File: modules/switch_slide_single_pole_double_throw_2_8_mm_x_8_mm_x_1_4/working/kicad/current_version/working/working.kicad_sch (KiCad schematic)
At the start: 1 part, among them J1 sws2880

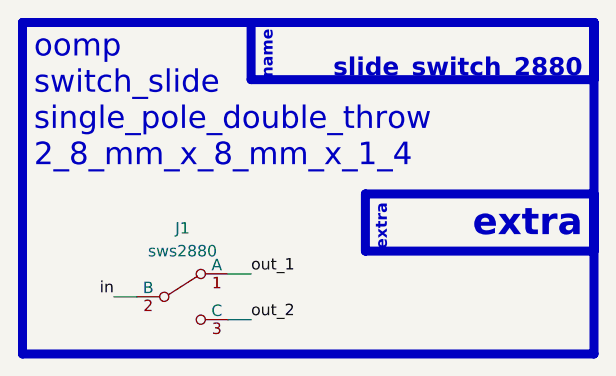
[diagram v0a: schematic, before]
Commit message: fixed formatting to be more consistent
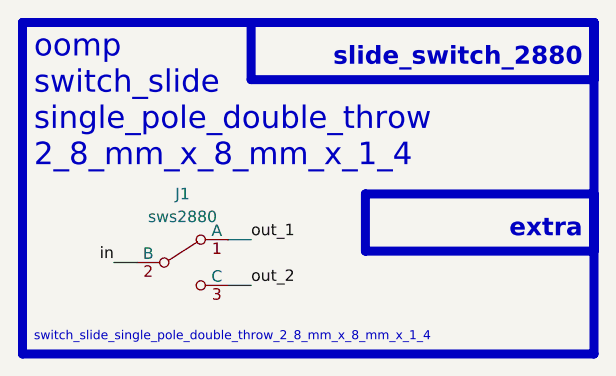
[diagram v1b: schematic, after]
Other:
- note added: "switch_slide_single_pole_double_throw_2_8_mm_x_8_mm_x_1_4"
- note removed: "name"
- moved on the sheet: J1
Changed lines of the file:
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@@
 (kicad_sch (version 20230121) (generator eeschema)
   (paper "A4")
-  (wire (pts (xy 116.84 86.36) (xy 119.38 86.36))
+  (wire (pts (xy 116.84 82.55) (xy 119.38 82.55))
     (stroke (width 0) (type default))
   )
-  (wire (pts (xy 129.54 88.9) (xy 132.08 88.9))
+  (wire (pts (xy 129.54 85.09) (xy 132.08 85.09))
     (stroke (width 0) (type default))
   )
-  (wire (pts (xy 129.54 83.82) (xy 132.08 83.82))
+  (wire (pts (xy 129.54 80.01) (xy 132.08 80.01))
     (stroke (width 0) (type default))
   )
   (rectangle (start 132.08 55.88) (end 170.18 62.23)
     (stroke (width 1) (type default))
-    (fill (type color) (color 0 0 0 0))
+    (fill (type none))
   )
   (rectangle (start 106.68 55.88) (end 170.18 92.71)
@@
     (fill (type none))
   )
-  (text "name" (at 134.62 62.23 90)
-    (effects (font (size 1.27 1.27) (thickness 0.254) bold (color 255 255 255 1)) (justify left bottom))
+  (text "slide_switch_2880" (at 168.91 60.96 0)
+    (effects (font (size 2 2) (thickness 0.8) bold) (justify right bottom))
   )
-  (text "slide_switch_2880" (at 168.91 62.23 0)
-    (effects (font (size 2 2) (thickness 0.8) bold (color 255 255 255 1)) (justify right bottom))
-  )
-  (text "extra" (at 147.32 81.28 90)
-    (effects (font (size 1.27 1.27) (thickness 0.254) bold) (justify left bottom))
+  (text "switch_slide_single_pole_double_throw_2_8_mm_x_8_mm_x_1_4"
+    (at 107.95 91.44 0)
+    (effects (font (size 1 1)) (justify left bottom))
   )
   (text "extra" (at 168.91 80.01 0)
-    (effects (font (size 3 3) (thickness 0.8) bold) (justify right bottom))
+    (effects (font (size 2 2) (thickness 0.8) bold) (justify right bottom))
   )
   (text "oomp\nswitch_slide\nsingle_pole_double_throw\n2_8_mm_x_8_mm_x_1_4\n\n"
@@
     (effects (font (size 2.5 2.5)) (justify left bottom))
   )
-  (label "out_1" (at 132.08 83.82 0) (fields_autoplaced)
+  (label "out_1" (at 132.08 80.01 0) (fields_autoplaced)
     (effects (font (size 1.27 1.27)) (justify left bottom))
   )
-  (label "out_2" (at 132.08 88.9 0) (fields_autoplaced)
+  (label "out_2" (at 132.08 85.09 0) (fields_autoplaced)
     (effects (font (size 1.27 1.27)) (justify left bottom))
   )
-  (label "in" (at 116.84 86.36 180) (fields_autoplaced)
+  (label "in" (at 116.84 82.55 180) (fields_autoplaced)
     (effects (font (size 1.27 1.27)) (justify right bottom))
   )
-  (symbol (lib_id "oomlout_oomp_part_symbols:sws2880_electronic_switch_slide_2_8_mm_x_8_mm_x_1_4_single_pole_double_throw") (at 124.46 86.36 0) (unit 1)
+  (symbol (lib_id "oomlout_oomp_part_symbols:sws2880_electronic_switch_slide_2_8_mm_x_8_mm_x_1_4_single_pole_double_throw") (at 124.46 82.55 0) (unit 1)
     (in_bom yes) (on_board yes) (dnp no) (fields_autoplaced)
-    (property "Reference" "J1" (at 124.46 78.74 0)
+    (property "Reference" "J1" (at 124.46 74.93 0)
       (effects (font (size 1.27 1.27)))
     )
-    (property "Value" "sws2880" (at 124.46 81.28 0)
+    (property "Value" "sws2880" (at 124.46 77.47 0)
       (effects (font (size 1.27 1.27)))
     )
-    (property "Footprint" "oomlout_oomp_part_footprints:sws2880_electronic_switch_slide_2_8_mm_x_8_mm_x_1_4_single_pole_double_throw" (at 124.46 86.36 0)
+    (property "Footprint" "oomlout_oomp_part_footprints:sws2880_electronic_switch_slide_2_8_mm_x_8_mm_x_1_4_single_pole_double_throw" (at 124.46 82.55 0)
       (effects (font (size 1.27 1.27)) hide)
     )
-    (property "Datasheet" "https://github.com/oomlout/oomlout_oomp_v3/parts/electronic_switch_slide_2_8_mm_x_8_mm_x_1_4_single_pole_double_throw/datasheet.pdf" (at 124.46 86.36 0)
+    (property "Datasheet" "https://github.com/oomlout/oomlout_oomp_v3/parts/electronic_switch_slide_2_8_mm_x_8_mm_x_1_4_single_pole_double_throw/datasheet.pdf" (at 124.46 82.55 0)
       (effects (font (size 1.27 1.27)) hide)
     )

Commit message: a few fix ups
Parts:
- renumbered J1 to SW1
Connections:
- net in renamed slide_switch_in
- net out_1 renamed slide_switch_out_1
- net out_2 renamed slide_switch_out_2
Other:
- moved on the sheet: SW1
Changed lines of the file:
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@@
 (kicad_sch (version 20230121) (generator eeschema)
   (paper "A4")
-  (wire (pts (xy 116.84 82.55) (xy 119.38 82.55))
+  (wire (pts (xy 128.27 93.98) (xy 130.81 93.98))
     (stroke (width 0) (type default))
   )
-  (wire (pts (xy 129.54 85.09) (xy 132.08 85.09))
+  (wire (pts (xy 140.97 96.52) (xy 143.51 96.52))
     (stroke (width 0) (type default))
   )
-  (wire (pts (xy 129.54 80.01) (xy 132.08 80.01))
+  (wire (pts (xy 140.97 91.44) (xy 143.51 91.44))
     (stroke (width 0) (type default))
   )
@@
     (fill (type none))
   )
-  (rectangle (start 106.68 55.88) (end 170.18 92.71)
+  (rectangle (start 106.68 55.88) (end 170.18 105.41)
     (stroke (width 1) (type default))
     (fill (type none))
   )
-  (rectangle (start 144.78 74.93) (end 170.18 81.28)
+  (rectangle (start 132.08 74.93) (end 170.18 81.28)
     (stroke (width 1) (type default))
     (fill (type none))
@@
   )
   (text "switch_slide_single_pole_double_throw_2_8_mm_x_8_mm_x_1_4"
-    (at 107.95 91.44 0)
+    (at 107.95 104.14 0)
     (effects (font (size 1 1)) (justify left bottom))
   )
@@
     (effects (font (size 2.5 2.5)) (justify left bottom))
   )
-  (label "out_1" (at 132.08 80.01 0) (fields_autoplaced)
+  (label "slide_switch_out_1" (at 143.51 91.44 0) (fields_autoplaced)
     (effects (font (size 1.27 1.27)) (justify left bottom))
   )
-  (label "out_2" (at 132.08 85.09 0) (fields_autoplaced)
+  (label "slide_switch_out_2" (at 143.51 96.52 0) (fields_autoplaced)
     (effects (font (size 1.27 1.27)) (justify left bottom))
   )
-  (label "in" (at 116.84 82.55 180) (fields_autoplaced)
+  (label "slide_switch_in" (at 128.27 93.98 180) (fields_autoplaced)
     (effects (font (size 1.27 1.27)) (justify right bottom))
   )
-  (symbol (lib_id "oomlout_oomp_part_symbols:sws2880_electronic_switch_slide_2_8_mm_x_8_mm_x_1_4_single_pole_double_throw") (at 124.46 82.55 0) (unit 1)
+  (symbol (lib_id "oomlout_oomp_part_symbols:sws2880_electronic_switch_slide_2_8_mm_x_8_mm_x_1_4_single_pole_double_throw") (at 135.89 93.98 0) (unit 1)
     (in_bom yes) (on_board yes) (dnp no) (fields_autoplaced)
-    (property "Reference" "J1" (at 124.46 74.93 0)
+    (property "Reference" "SW1" (at 135.89 86.36 0)
       (effects (font (size 1.27 1.27)))
     )
-    (property "Value" "sws2880" (at 124.46 77.47 0)
+    (property "Value" "sws2880" (at 135.89 88.9 0)
       (effects (font (size 1.27 1.27)))
     )
-    (property "Footprint" "oomlout_oomp_part_footprints:sws2880_electronic_switch_slide_2_8_mm_x_8_mm_x_1_4_single_pole_double_throw" (at 124.46 82.55 0)
+    (property "Footprint" "oomlout_oomp_part_footprints:sws2880_electronic_switch_slide_2_8_mm_x_8_mm_x_1_4_single_pole_double_throw" (at 135.89 93.98 0)
       (effects (font (size 1.27 1.27)) hide)
     )
-    (property "Datasheet" "https://github.com/oomlout/oomlout_oomp_v3/parts/electronic_switch_slide_2_8_mm_x_8_mm_x_1_4_single_pole_double_throw/datasheet.pdf" (at 124.46 82.55 0)
+    (property "Datasheet" "https://github.com/oomlout/oomlout_oomp_v3/parts/electronic_switch_slide_2_8_mm_x_8_mm_x_1_4_single_pole_double_throw/datasheet.pdf" (at 135.89 93.98 0)
       (effects (font (size 1.27 1.27)) hide)
     )
@@
       (project "working"
         (path "/c9993764-076f-44f6-bf4c-6b69ce17c9e4"
-          (reference "J1") (unit 1)
+          (reference "SW1") (unit 1)
         )
       )

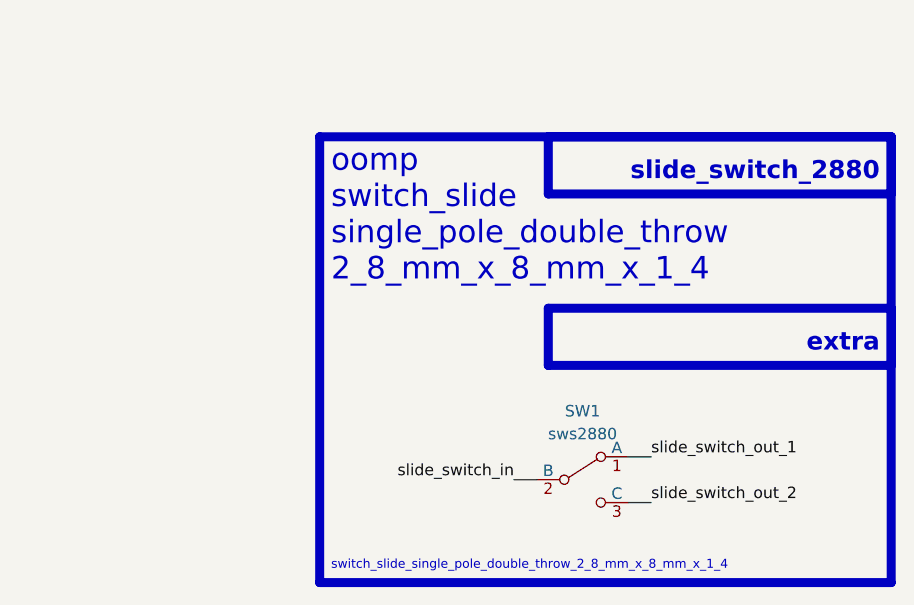
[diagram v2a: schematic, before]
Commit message: schematic formatting
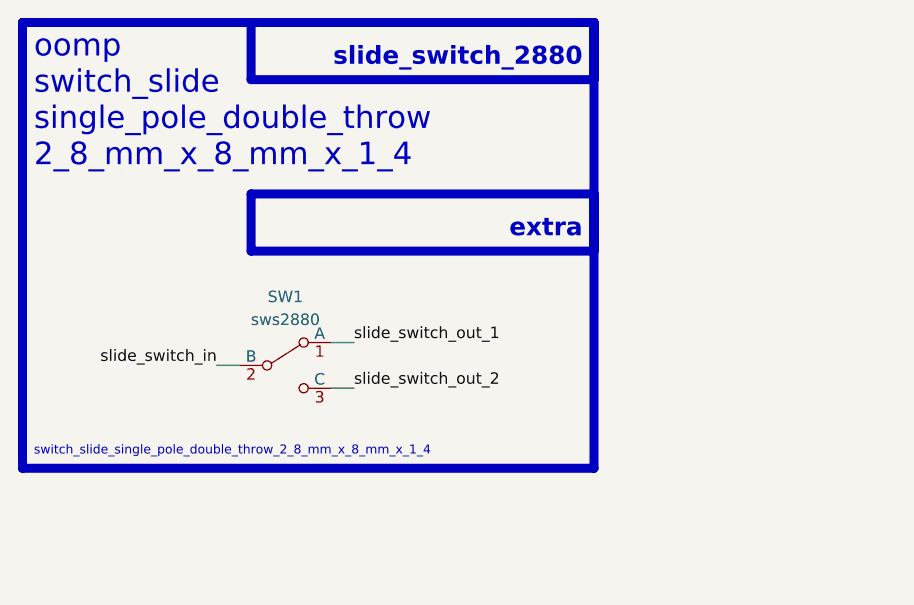
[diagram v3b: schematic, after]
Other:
- moved on the sheet: SW1
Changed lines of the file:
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@@
 (kicad_sch (version 20230121) (generator eeschema)
-  (paper "A4")
-  (wire (pts (xy 128.27 93.98) (xy 130.81 93.98))
+  (paper "A5")
+  (wire (pts (xy 95.25 81.28) (xy 97.79 81.28))
     (stroke (width 0) (type default))
   )
-  (wire (pts (xy 140.97 96.52) (xy 143.51 96.52))
+  (wire (pts (xy 107.95 83.82) (xy 110.49 83.82))
     (stroke (width 0) (type default))
   )
-  (wire (pts (xy 140.97 91.44) (xy 143.51 91.44))
+  (wire (pts (xy 107.95 78.74) (xy 110.49 78.74))
     (stroke (width 0) (type default))
   )
-  (rectangle (start 132.08 55.88) (end 170.18 62.23)
+  (rectangle (start 99.06 43.18) (end 137.16 49.53)
     (stroke (width 1) (type default))
     (fill (type none))
   )
-  (rectangle (start 106.68 55.88) (end 170.18 105.41)
+  (rectangle (start 73.66 43.18) (end 137.16 92.71)
     (stroke (width 1) (type default))
     (fill (type none))
   )
-  (rectangle (start 132.08 74.93) (end 170.18 81.28)
+  (rectangle (start 99.06 62.23) (end 137.16 68.58)
     (stroke (width 1) (type default))
     (fill (type none))
   )
-  (rectangle (start 151.13 219.71) (end 151.13 219.71)
+  (rectangle (start 118.11 207.01) (end 118.11 207.01)
     (stroke (width 0) (type default))
     (fill (type none))
   )
-  (text "slide_switch_2880" (at 168.91 60.96 0)
+  (text "slide_switch_2880" (at 135.89 48.26 0)
     (effects (font (size 2 2) (thickness 0.8) bold) (justify right bottom))
   )
   (text "switch_slide_single_pole_double_throw_2_8_mm_x_8_mm_x_1_4"
-    (at 107.95 104.14 0)
+    (at 74.93 91.44 0)
     (effects (font (size 1 1)) (justify left bottom))
   )
-  (text "extra" (at 168.91 80.01 0)
+  (text "extra" (at 135.89 67.31 0)
     (effects (font (size 2 2) (thickness 0.8) bold) (justify right bottom))
   )
   (text "oomp\nswitch_slide\nsingle_pole_double_throw\n2_8_mm_x_8_mm_x_1_4\n\n"
-    (at 107.95 76.2 0)
+    (at 74.93 63.5 0)
     (effects (font (size 2.5 2.5)) (justify left bottom))
   )
-  (label "slide_switch_out_1" (at 143.51 91.44 0) (fields_autoplaced)
+  (label "slide_switch_out_1" (at 110.49 78.74 0) (fields_autoplaced)
     (effects (font (size 1.27 1.27)) (justify left bottom))
   )
-  (label "slide_switch_out_2" (at 143.51 96.52 0) (fields_autoplaced)
+  (label "slide_switch_out_2" (at 110.49 83.82 0) (fields_autoplaced)
     (effects (font (size 1.27 1.27)) (justify left bottom))
   )
-  (label "slide_switch_in" (at 128.27 93.98 180) (fields_autoplaced)
+  (label "slide_switch_in" (at 95.25 81.28 180) (fields_autoplaced)
     (effects (font (size 1.27 1.27)) (justify right bottom))
   )
-  (symbol (lib_id "oomlout_oomp_part_symbols:sws2880_electronic_switch_slide_2_8_mm_x_8_mm_x_1_4_single_pole_double_throw") (at 135.89 93.98 0) (unit 1)
+  (symbol (lib_id "oomlout_oomp_part_symbols:sws2880_electronic_switch_slide_2_8_mm_x_8_mm_x_1_4_single_pole_double_throw") (at 102.87 81.28 0) (unit 1)
     (in_bom yes) (on_board yes) (dnp no) (fields_autoplaced)
-    (property "Reference" "SW1" (at 135.89 86.36 0)
+    (property "Reference" "SW1" (at 102.87 73.66 0)
       (effects (font (size 1.27 1.27)))
     )
-    (property "Value" "sws2880" (at 135.89 88.9 0)
+    (property "Value" "sws2880" (at 102.87 76.2 0)
       (effects (font (size 1.27 1.27)))
     )
-    (property "Footprint" "oomlout_oomp_part_footprints:sws2880_electronic_switch_slide_2_8_mm_x_8_mm_x_1_4_single_pole_double_throw" (at 135.89 93.98 0)
+    (property "Footprint" "oomlout_oomp_part_footprints:sws2880_electronic_switch_slide_2_8_mm_x_8_mm_x_1_4_single_pole_double_throw" (at 102.87 81.28 0)
       (effects (font (size 1.27 1.27)) hide)
     )
-    (property "Datasheet" "https://github.com/oomlout/oomlout_oomp_v3/parts/electronic_switch_slide_2_8_mm_x_8_mm_x_1_4_single_pole_double_throw/datasheet.pdf" (at 135.89 93.98 0)
+    (property "Datasheet" "https://github.com/oomlout/oomlout_oomp_v3/parts/electronic_switch_slide_2_8_mm_x_8_mm_x_1_4_single_pole_double_throw/datasheet.pdf" (at 102.87 81.28 0)
       (effects (font (size 1.27 1.27)) hide)
     )
